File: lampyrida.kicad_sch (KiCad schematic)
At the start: 15 parts, among them K1 SW_Push_45deg, K2 SW_Push_45deg, K3 SW_Push_45deg, K4 SW_Push_45deg, U1 RP2040 Zero

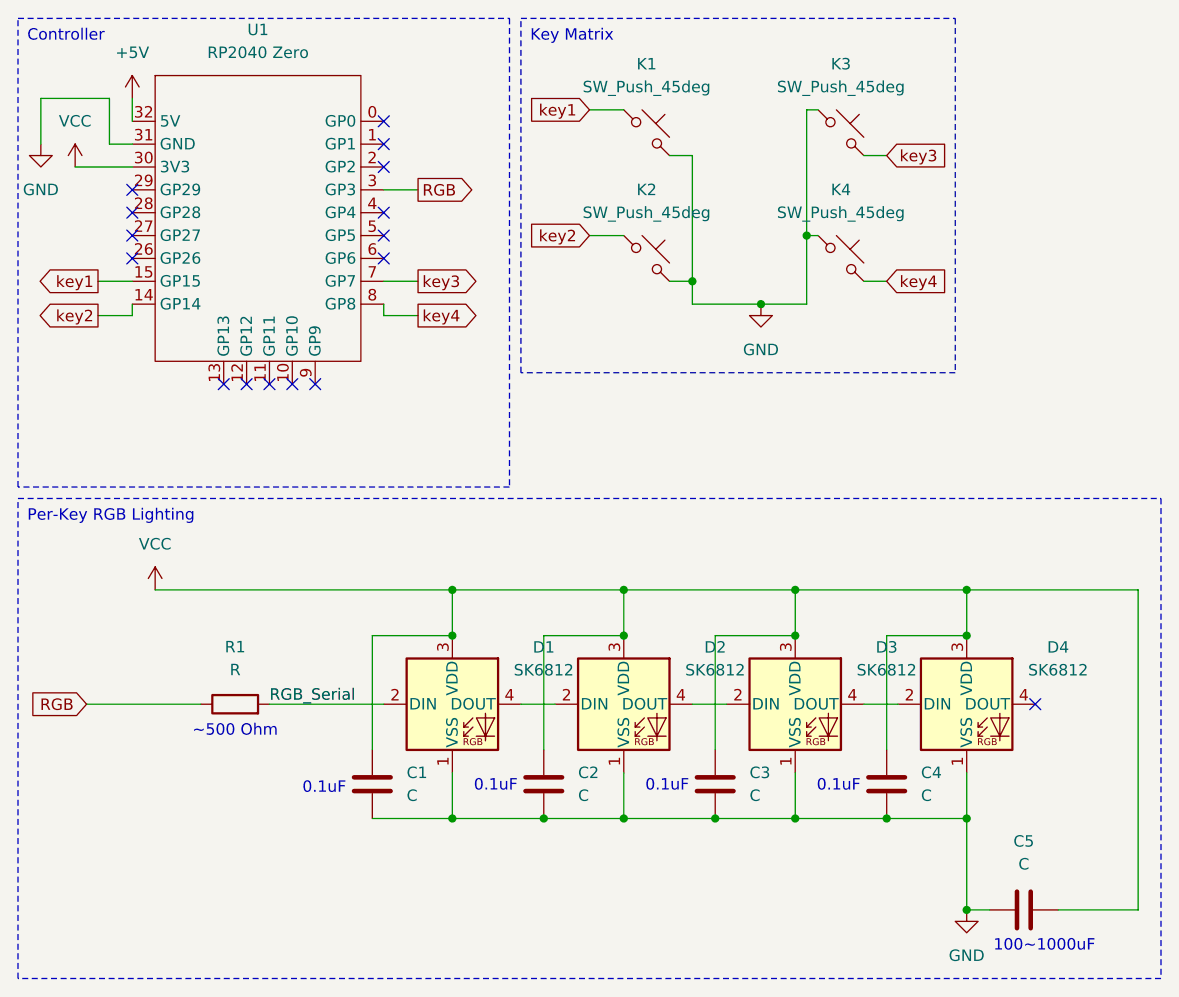
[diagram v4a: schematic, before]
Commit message: Fixing SK6812-MiniE footprint and rerouting traces to match.
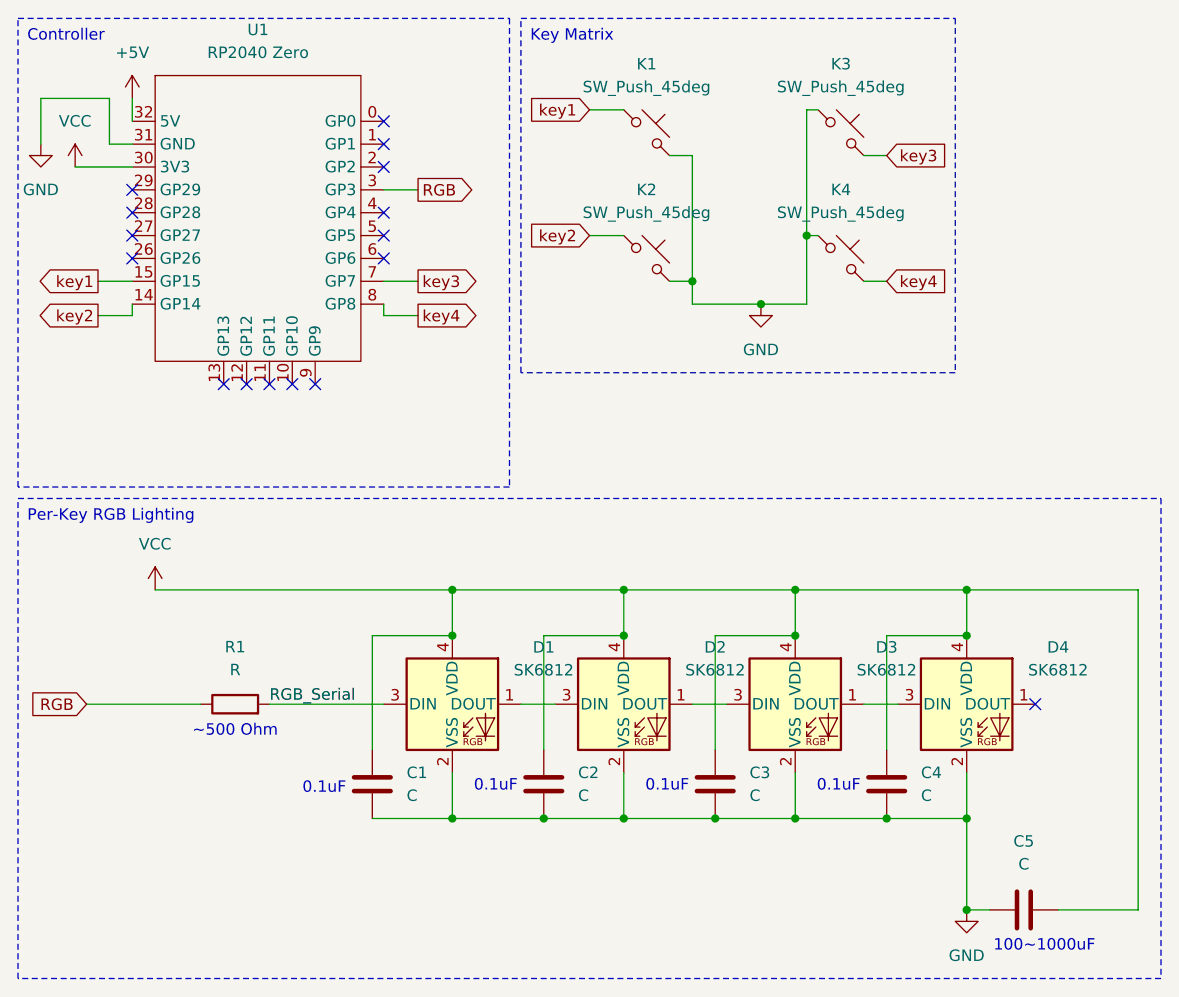
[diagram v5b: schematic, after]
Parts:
- D1, D2, D3, D4: footprint LED_SMD:LED_SK6812_PLCC4_5.0x5.0mm_P3.2mm -> keyboard_parts:LED_RGB_SK6812Mini-E; symbol LED:SK6812 -> LED:SK6812MINI
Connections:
- net GND: now also D1.2 (VSS), D2.2 (VSS), D3.2 (VSS), D4.2 (VSS); no longer D1.1 (VSS), D2.1 (VSS), D3.1 (VSS), D4.1 (VSS)
- net RGB_Serial: now also D1.3 (DIN); no longer D1.2 (DIN)
- net VCC: now also D1.4 (VDD), D2.4 (VDD), D3.4 (VDD), D4.4 (VDD); no longer D1.3 (VDD), D2.3 (VDD), D3.3 (VDD), D4.3 (VDD)
- new net: D2.1 (DOUT), D3.3 (DIN)
- new net: D1.1 (DOUT), D2.3 (DIN)
- new net: D3.1 (DOUT), D4.3 (DIN)
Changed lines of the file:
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@@
 	)
 	(symbol
-		(lib_id "LED:SK6812")
+		(lib_id "LED:SK6812MINI")
 		(at 83.82 91.44 0)
 		(unit 1)
@@
 			)
 		)
-		(property "Footprint" "LED_SMD:LED_SK6812_PLCC4_5.0x5.0mm_P3.2mm"
+		(property "Footprint" "keyboard_parts:LED_RGB_SK6812Mini-E"
 			(at 85.09 99.06 0)
 			(effects
@@
 			)
 		)
-		(property "Datasheet" "https://cdn-shop.adafruit.com/product-files/1138/SK6812+LED+datasheet+.pdf"
+		(property "Datasheet" "https://cdn-shop.adafruit.com/product-files/2686/SK6812MINI_REV.01-1-2.pdf"
 			(at 86.36 100.965 0)
 			(effects
@@
 	)
 	(symbol
-		(lib_id "LED:SK6812")
+		(lib_id "LED:SK6812MINI")
 		(at 102.87 91.44 0)
 		(unit 1)
@@
 			)
 		)
-		(property "Footprint" "LED_SMD:LED_SK6812_PLCC4_5.0x5.0mm_P3.2mm"
+		(property "Footprint" "keyboard_parts:LED_RGB_SK6812Mini-E"
 			(at 104.14 99.06 0)
 			(effects
@@
 			)
 		)
-		(property "Datasheet" "https://cdn-shop.adafruit.com/product-files/1138/SK6812+LED+datasheet+.pdf"
+		(property "Datasheet" "https://cdn-shop.adafruit.com/product-files/2686/SK6812MINI_REV.01-1-2.pdf"
 			(at 105.41 100.965 0)
 			(effects
@@
 	)
 	(symbol
-		(lib_id "LED:SK6812")
+		(lib_id "LED:SK6812MINI")
 		(at 64.77 91.44 0)
 		(unit 1)
@@
 			)
 		)
-		(property "Footprint" "LED_SMD:LED_SK6812_PLCC4_5.0x5.0mm_P3.2mm"
+		(property "Footprint" "keyboard_parts:LED_RGB_SK6812Mini-E"
 			(at 66.04 99.06 0)
 			(effects
@@
 			)
 		)
-		(property "Datasheet" "https://cdn-shop.adafruit.com/product-files/1138/SK6812+LED+datasheet+.pdf"
+		(property "Datasheet" "https://cdn-shop.adafruit.com/product-files/2686/SK6812MINI_REV.01-1-2.pdf"
 			(at 67.31 100.965 0)
 			(effects
@@
 	)
 	(symbol
-		(lib_id "LED:SK6812")
+		(lib_id "LED:SK6812MINI")
 		(at 121.92 91.44 0)
 		(unit 1)
@@
 			)
 		)
-		(property "Footprint" "LED_SMD:LED_SK6812_PLCC4_5.0x5.0mm_P3.2mm"
+		(property "Footprint" "keyboard_parts:LED_RGB_SK6812Mini-E"
 			(at 123.19 99.06 0)
 			(effects
@@
 			)
 		)
-		(property "Datasheet" "https://cdn-shop.adafruit.com/product-files/1138/SK6812+LED+datasheet+.pdf"
+		(property "Datasheet" "https://cdn-shop.adafruit.com/product-files/2686/SK6812MINI_REV.01-1-2.pdf"
 			(at 124.46 100.965 0)
 			(effects

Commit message: Correcting DRC violations.
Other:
- title: (none) -> Lampyrida
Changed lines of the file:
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@@
 	(generator_version "8.0")
 	(paper "A4")
+	(title_block
+		(title "Lampyrida")
+		(date "2025-05-18")
+		(rev "0.0.3")
+	)
 	(junction
 		(at 91.44 44.45)
